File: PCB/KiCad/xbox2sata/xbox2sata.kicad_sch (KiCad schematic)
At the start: 47 parts, among them J1 929975-01-20-RK, J2 61203921621, J3 SATA-A-PL-SMT-K, U1 1V2 voltage regulator, U5 88SA8052, Y1 25MHz

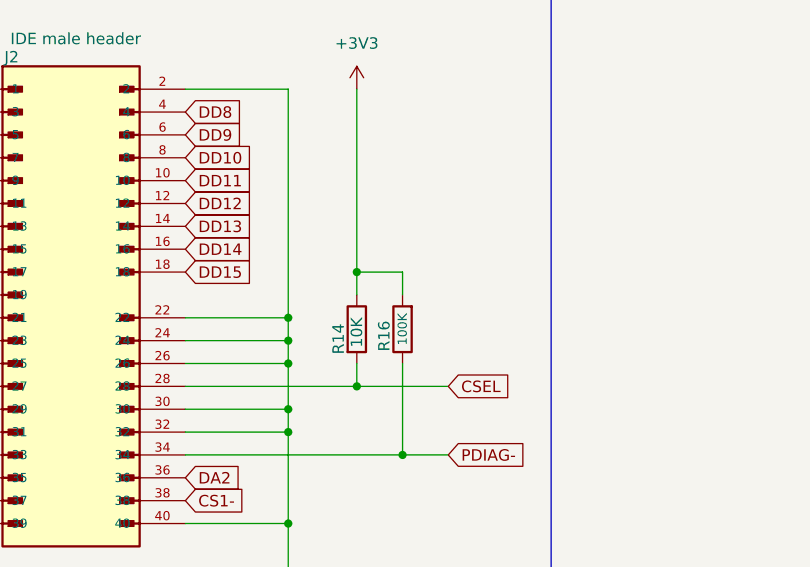
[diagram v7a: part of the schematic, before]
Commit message: why u not work!?!
going back from start checking for errors, but I'm guessing the error lies with the IDE pull-up and down resistors and possibly the T0-8 configuration setup.
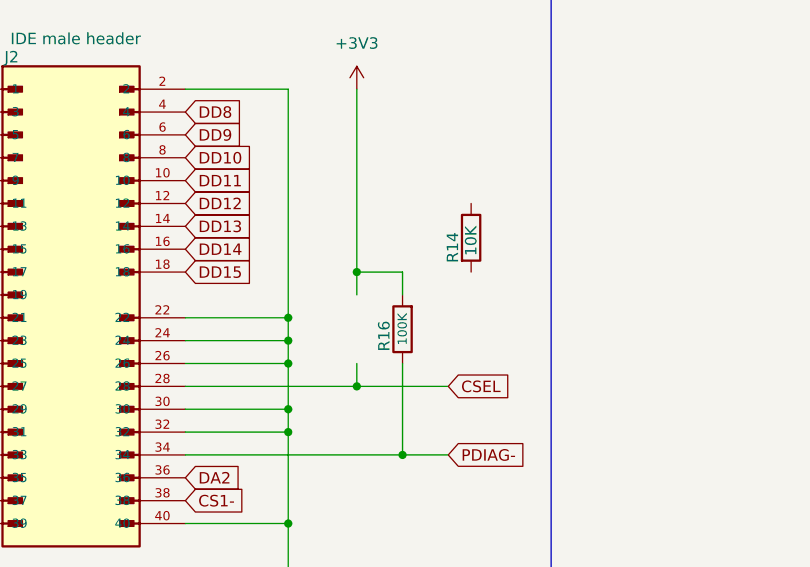
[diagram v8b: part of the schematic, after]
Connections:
- net +3V3: no longer R14.1
- net CSEL: no longer R14.2
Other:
- moved on the sheet: R14
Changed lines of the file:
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@@
 	(symbol
 		(lib_id "Device:R")
-		(at 200.66 135.89 0)
+		(at 213.36 125.73 0)
 		(unit 1)
 		(exclude_from_sim no)
@@
 		(dnp no)
 		(property "Reference" "R14"
-			(at 198.628 138.684 90)
+			(at 211.328 128.524 90)
 			(effects
 				(font
@@
 		)
 		(property "Value" "10K"
-			(at 200.66 137.922 90)
+			(at 213.36 127.762 90)
 			(effects
 				(font
@@
 		)
 		(property "Footprint" "Resistor_SMD:R_0402_1005Metric_Pad0.72x0.64mm_HandSolder"
-			(at 198.882 135.89 90)
+			(at 211.582 125.73 90)
 			(effects
 				(font
@@
 		)
 		(property "Datasheet" "~"
-			(at 200.66 135.89 0)
+			(at 213.36 125.73 0)
 			(effects
 				(font
@@
 		)
 		(property "Description" "Resistor"
-			(at 200.66 135.89 0)
+			(at 213.36 125.73 0)
 			(effects
 				(font
